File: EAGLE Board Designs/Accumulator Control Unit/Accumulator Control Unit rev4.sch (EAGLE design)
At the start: 244 parts, among them J1 CONNECTOR-2_MF_T_V_, J100 CONNECTOR-8_NF_T_V_NATURAL, J2 CONNECTOR-8_MF_T_V_, J3 CONNECTOR-14_MF_T_V_, J4 JUMPER__1X02, J5 CONNECTOR-12_MF_T_V_, J6 CONNECTOR-CAN_μF_S_RA_, J7 CONNECTOR-2_MOLEX_NANOFIT_PTH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, J8 JUMPER__1X02, K1 RELAY_SOLIDSTATE_NO_CPC1020NTR, Q1 TRANSISTOR_N_MOS__PMV15ENEA, Q100 TRANSISTOR_N_MOS__PMV15ENEA, Q101 TRANSISTOR_N_MOS__PMV15ENEA, Q2 TRANSISTOR_N_MOS__PMV15ENEA, T1 TRANSFORMER_HM2112ZNLT_AIRGAP, U1 RELAY_SOLIDSTATE_NO_DIP-4, U10 MAX7404, U100 ADG1423, U101 LM555, U11 OPAMP_1_CHANNEL_OPA991, U12 LOGICGATE_AND_DCK3, U13 OPAMP_1_CHANNEL_OPA991, U14 LOGICGATE_AND_DCK3, U15 OPAMP_1_CHANNEL_OPA991, U16 LOGICGATE_AND_DCK3, U17 OPAMP_1_CHANNEL_OPA991, U18 OPAMP_1_CHANNEL_OPA991, U19 MAX7404, U2 RELAY_SOLIDSTATE_NO_DIP-4, U20 OPAMP_1_CHANNEL_OPA991, U21 OPAMP_1_CHANNEL_OPA991, U22 OPAMP_1_CHANNEL_OPA991, U23 OPAMP_1_CHANNEL_OPA991, U24 OPAMP_1_CHANNEL_OPA991, U25 MAX7404, U26 VOLTAGE_REGULATOR_SOT-223_3.3V, U27 TCAN1051HQV-Q1, U28 OPAMP_1_CHANNEL_OPA991, U29 TCAN1051HQV-Q1, U3 OPAMP_1_CHANNEL_OPA991, U4 MAX7404, U5 LTC6820, U6 LOGICGATE_BUFFER, U7 ADM8316WBX30, U8 RELAY_SOLIDSTATE_NO_DIP-4, U9 OPAMP_1_CHANNEL_OPA991

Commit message: changes in progress
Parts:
- removed J7: CONNECTOR-2_MOLEX_NANOFIT_PTH_VERTICAL_02_BLACK, HyTechDevices:CONNECTOR-2_MOLEX_NANOFIT_PTH_VERTICAL_02_BLACK
- J5: value CONNECTOR-12_MF_T_V_ -> CONNECTOR-14_MF_T_V_; device HyTechDevices - Copy:CONNECTOR-12_MF_T_V_ -> HyTechDevices:CONNECTOR-14_MF_T_V_
- J6: value CONNECTOR-CAN_μF_S_RA_ -> CONNECTOR-4_μF_T_V_BLACK; device HyTechDevices:CONNECTOR-CAN_μF_S_RA_ -> HyTechDevices:CONNECTOR-4_μF_T_V_BLACK
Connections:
- net +24V: now also J6.1; no longer J5.1, J6.+24V
- net 24VIN: now also J5.1; no longer J7.1
- net CHASSIS_GND: now also J5.13; no longer J7.2
- net EM_CANH: now also J6.2; no longer J6.CANH
- net EM_CANL: now also J6.3; no longer J6.CANL
- net GND: now also J6.4; no longer J6.GND
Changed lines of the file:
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@@
 <part name="D4" library="HyTechDevices - Copy" deviceset="TVS_*" device="" technology="8V"/>
 <part name="P5" library="HyTechSupplies" deviceset="GND" device=""/>
-<part name="J6" library="HyTechDevices" deviceset="CONNECTOR-CAN_?_*" device="μF_S_RA"/>
-<part name="J5" library="HyTechDevices - Copy" deviceset="CONNECTOR-12_?_*" device="MF_T_V"/>
+<part name="J5" library="HyTechDevices" deviceset="CONNECTOR-14_?_*" device="MF_T_V"/>
 <part name="R12" library="HyTechDevices" deviceset="RESISTOR_?_*" device="0603" technology="20K" value="RESISTOR_0603_20K"/>
 <part name="GND5" library="supply1" library_urn="urn:adsk.eagle:library:371" deviceset="GND" device=""/>
@@
 <part name="R75" library="HyTechDevices" deviceset="RESISTOR_?_*" device="0603" technology="10.5K"/>
 <part name="R76" library="HyTechDevices" deviceset="RESISTOR_?_*" device="0603" technology="10.5K"/>
-<part name="U$29" library="HyTechSupplies" deviceset="+24V" device=""/>
-<part name="J7" library="HyTechDevices" deviceset="CONNECTOR-2_?_*" device="MOLEX_NANOFIT_PTH_VERTICAL_02" technology="BLACK"/>
 <part name="P115" library="HyTechSupplies" deviceset="GND" device=""/>
 <part name="U29" library="HyTechDevices" deviceset="TCAN1051*V-Q1" device="" technology="HQ"/>
@@
 <part name="P11" library="HyTechSupplies" deviceset="GND" device=""/>
 <part name="R92" library="HyTechDevices" deviceset="RESISTOR_?_*" device="0603" technology="10K"/>
+<part name="J6" library="HyTechDevices" deviceset="CONNECTOR-4_?_*" device="μF_T_V" technology="BLACK"/>
 </parts>
 <sheets>
@@
 <attribute name="VALUE" x="27.94" y="143.51" size="1.27" layer="96" align="top-center"/>
 </instance>
-<instance part="J6" gate="G$1" x="10.16" y="195.58" smashed="yes">
-<attribute name="NAME" x="10.16" y="196.215" size="1.27" layer="95"/>
-<attribute name="MPN" x="10.16" y="182.245" size="1.27" layer="96" align="top-left"/>
-</instance>
 <instance part="J5" gate="G$1" x="58.42" y="187.96" smashed="yes">
 <attribute name="NAME" x="58.42" y="188.722" size="1.778" layer="95"/>
-<attribute name="MPN" x="58.42" y="154.305" size="1.27" layer="96" align="top-left"/>
+<attribute name="MPN" x="58.42" y="149.225" size="1.27" layer="96" align="top-left"/>
 </instance>
 <instance part="P8" gate="G$1" x="27.94" y="68.58" smashed="yes">
@@
 <attribute name="VALUE" x="43.18" y="124.46" size="1.27" layer="96" align="bottom-center"/>
 </instance>
-<instance part="U$29" gate="G$1" x="83.82" y="187.96" smashed="yes">
-<attribute name="VALUE" x="83.82" y="193.04" size="1.778" layer="96" align="bottom-center"/>
-</instance>
-<instance part="J7" gate="G$1" x="58.42" y="142.24" smashed="yes">
-<attribute name="MPN" x="58.42" y="133.985" size="1.27" layer="96" align="top-left"/>
-<attribute name="NAME" x="58.42" y="143.002" size="1.27" layer="95"/>
-</instance>
-<instance part="P115" gate="1" x="76.2" y="152.4" smashed="yes">
-<attribute name="VALUE" x="76.2" y="151.13" size="1.27" layer="96" align="top-center"/>
+<instance part="P115" gate="1" x="93.98" y="154.94" smashed="yes">
+<attribute name="VALUE" x="93.98" y="153.67" size="1.27" layer="96" align="top-center"/>
 </instance>
 <instance part="K1" gate="G$1" x="83.82" y="58.42" smashed="yes">
@@
 <attribute name="NAME" x="74.93" y="57.15" size="1.27" layer="95" align="bottom-center"/>
 <attribute name="RESISTANCE" x="74.93" y="54.61" size="1.27" layer="96" align="top-center"/>
+</instance>
+<instance part="J6" gate="G$1" x="12.7" y="195.58" smashed="yes">
+<attribute name="MPN" x="12.7" y="182.245" size="1.27" layer="96" align="top-left"/>
+<attribute name="NAME" x="12.7" y="196.342" size="1.27" layer="95"/>
 </instance>
 </instances>
@@
 <wire x1="22.86" y1="185.42" x2="27.94" y2="185.42" width="0.1524" layer="91"/>
 <wire x1="27.94" y1="185.42" x2="27.94" y2="182.88" width="0.1524" layer="91"/>
-<pinref part="J6" gate="G$1" pin="GND"/>
+<pinref part="J6" gate="G$1" pin="4"/>
 </segment>
 <segment>
@@
 <pinref part="J5" gate="G$1" pin="12"/>
 <pinref part="P115" gate="1" pin="GND"/>
-<wire x1="68.58" y1="157.48" x2="76.2" y2="157.48" width="0.1524" layer="91"/>
-<wire x1="76.2" y1="157.48" x2="76.2" y2="154.94" width="0.1524" layer="91"/>
+<wire x1="68.58" y1="157.48" x2="93.98" y2="157.48" width="0.1524" layer="91"/>
 </segment>
 <segment>
@@
 </segment>
 <segment>
-<pinref part="J7" gate="G$1" pin="1"/>
-<wire x1="68.58" y1="139.7" x2="71.12" y2="139.7" width="0.1524" layer="91"/>
-<label x="71.12" y="139.7" size="1.27" layer="95" xref="yes"/>
+<pinref part="J5" gate="G$1" pin="1"/>
+<wire x1="68.58" y1="185.42" x2="83.82" y2="185.42" width="0.1524" layer="91"/>
+<label x="83.82" y="185.42" size="1.27" layer="95" xref="yes"/>
 </segment>
 </net>
@@
 </segment>
 <segment>
-<pinref part="J7" gate="G$1" pin="2"/>
-<wire x1="68.58" y1="137.16" x2="71.12" y2="137.16" width="0.1524" layer="91"/>
-<label x="71.12" y="137.16" size="1.27" layer="95" xref="yes"/>
+<pinref part="J5" gate="G$1" pin="13"/>
+<wire x1="68.58" y1="154.94" x2="76.2" y2="154.94" width="0.1524" layer="91"/>
+<label x="76.2" y="154.94" size="1.27" layer="95" xref="yes"/>
 </segment>
 </net>
@@
 <segment>
 <pinref part="P1" gate="G$1" pin="+24V"/>
-<pinref part="J6" gate="G$1" pin="+24V"/>
 <wire x1="27.94" y1="195.58" x2="27.94" y2="193.04" width="0.1524" layer="91"/>
 <wire x1="27.94" y1="193.04" x2="22.86" y2="193.04" width="0.1524" layer="91"/>
+<pinref part="J6" gate="G$1" pin="1"/>
 </segment>
 <segment>
@@
 </segment>
 <segment>
-<pinref part="J5" gate="G$1" pin="1"/>
-<pinref part="U$29" gate="G$1" pin="+24V"/>
-<wire x1="68.58" y1="185.42" x2="83.82" y2="185.42" width="0.1524" layer="91"/>
-</segment>
-<segment>
 <pinref part="U$30" gate="G$1" pin="+24V"/>
 <pinref part="K1" gate="G$1" pin="CONTACT2"/>
@@
 <wire x1="22.86" y1="190.5" x2="25.4" y2="190.5" width="0.1524" layer="91"/>
 <label x="25.4" y="190.5" size="1.27" layer="95" xref="yes"/>
-<pinref part="J6" gate="G$1" pin="CANH"/>
+<pinref part="J6" gate="G$1" pin="2"/>
 </segment>
 </net>
@@
 <wire x1="22.86" y1="187.96" x2="25.4" y2="187.96" width="0.1524" layer="91"/>
 <label x="25.4" y="187.96" size="1.27" layer="95" xref="yes"/>
-<pinref part="J6" gate="G$1" pin="CANL"/>
-</segment>
-</net>
+<pinref part="J6" gate="G$1" pin="3"/>
+</segment>
+</net>

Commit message: wip
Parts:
- J3: value CONNECTOR-14_MF_T_V_ -> CONNECTOR-12_MF_T_V_; device HyTechDevices:CONNECTOR-14_MF_T_V_ -> HyTechDevices:CONNECTOR-12_MF_T_V_
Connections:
- new net N$40: J3.10
- net +24V: now also J3.5; no longer J3.7
- net +5V: now also J3.3; no longer J3.5
- net ACCUMULATOR_GND: now also J3.12; no longer J3.14
- net AIR2-: now also J3.11; no longer J3.13
- net CURRENT: now also J3.6; no longer J3.8
- net CURRENT_REF: now also J3.7; no longer J3.9
- net GND: now also J3.2, J3.9; no longer J3.11, J3.6
- net SHDN: now also J3.8; no longer J3.10, J3.12
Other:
- note added: "Current Sensor Accumulator GND, both AIR+ and -"
- note removed: "Energy Meter, Current Sensor Accumulator GND, both AIR+ and -"
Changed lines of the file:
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@@
 <layer number="56" name="wert" color="7" fill="1" visible="no" active="no"/>
 <layer number="57" name="tCAD" color="7" fill="1" visible="no" active="no"/>
+<layer number="58" name="bCAD" color="7" fill="1" visible="no" active="no"/>
 <layer number="59" name="tCarbon" color="7" fill="1" visible="no" active="no"/>
 <layer number="60" name="bCarbon" color="7" fill="1" visible="no" active="no"/>
@@
 <layer number="156" name="HVSpacing" color="12" fill="1" visible="no" active="yes"/>
 <layer number="157" name="HIGH_VOLTAGE_WIRES" color="2" fill="1" visible="yes" active="yes"/>
+<layer number="166" name="AntennaArea" color="7" fill="1" visible="no" active="no"/>
+<layer number="168" name="4mmHeightArea" color="7" fill="1" visible="no" active="no"/>
 <layer number="191" name="mNets" color="7" fill="1" visible="no" active="yes"/>
 <layer number="192" name="mBusses" color="7" fill="1" visible="no" active="yes"/>
@@
 <part name="P109" library="HyTechSupplies" deviceset="+24V" device=""/>
 <part name="TP1_24V" library="HyTechDevices" deviceset="TEST_POINT" device=""/>
-<part name="J3" library="HyTechDevices" deviceset="CONNECTOR-14_?_*" device="MF_T_V"/>
 <part name="U$21" library="HyTechSupplies" deviceset="+24V" device=""/>
 <part name="P110" library="HyTechSupplies" deviceset="GND" device=""/>
@@
 <part name="R92" library="HyTechDevices" deviceset="RESISTOR_?_*" device="0603" technology="10K"/>
 <part name="J6" library="HyTechDevices" deviceset="CONNECTOR-4_?_*" device="μF_T_V" technology="BLACK"/>
+<part name="J3" library="HyTechDevices" deviceset="CONNECTOR-12_?_*" device="MF_T_V"/>
 </parts>
 <sheets>
@@
 <text x="30.988" y="105.156" size="0.8128" layer="97">SHDN connnects directly
 to AIR+</text>
-<text x="7.62" y="134.62" size="1.778" layer="97">Energy Meter, Current Sensor
+<text x="7.62" y="134.62" size="1.778" layer="97">Current Sensor
 Accumulator GND, both AIR+ and -</text>
 <text x="7.62" y="71.12" size="1.778" layer="97">IMD</text>
@@
 <attribute name="MPN" x="193.04" y="196.342" size="1.27" layer="95" align="top-left"/>
 </instance>
-<instance part="J3" gate="G$1" x="10.16" y="132.08" smashed="yes">
-<attribute name="NAME" x="10.16" y="132.842" size="1.27" layer="95"/>
-<attribute name="MPN" x="10.16" y="93.345" size="1.27" layer="96" align="top-left"/>
-</instance>
 <instance part="U$21" gate="G$1" x="101.6" y="160.02" smashed="yes">
 <attribute name="VALUE" x="101.6" y="165.1" size="1.778" layer="96" align="bottom-center"/>
@@
 <attribute name="VOLTAGE" x="121.285" y="184.15" size="1.27" layer="96" rot="R90" align="top-center"/>
 </instance>
-<instance part="P7" gate="1" x="43.18" y="121.92" smashed="yes">
-<attribute name="VALUE" x="43.18" y="124.46" size="1.27" layer="96" align="bottom-center"/>
+<instance part="P7" gate="1" x="40.64" y="121.92" smashed="yes">
+<attribute name="VALUE" x="43.18" y="121.92" size="1.27" layer="96" align="bottom-center"/>
 </instance>
 <instance part="P115" gate="1" x="93.98" y="154.94" smashed="yes">
@@
 <attribute name="MPN" x="12.7" y="182.245" size="1.27" layer="96" align="top-left"/>
 <attribute name="NAME" x="12.7" y="196.342" size="1.27" layer="95"/>
+</instance>
+<instance part="J3" gate="G$1" x="10.16" y="127" smashed="yes">
+<attribute name="NAME" x="10.16" y="127.762" size="1.778" layer="95"/>
+<attribute name="MPN" x="10.16" y="93.345" size="1.27" layer="96" align="top-left"/>
 </instance>
 </instances>
@@
 <wire x1="20.32" y1="106.68" x2="22.86" y2="106.68" width="0.1524" layer="91"/>
 <label x="22.86" y="106.68" size="1.27" layer="95" xref="yes"/>
-<pinref part="J3" gate="G$1" pin="10"/>
-</segment>
-<segment>
-<wire x1="20.32" y1="101.6" x2="22.86" y2="101.6" width="0.1524" layer="91"/>
-<label x="22.86" y="101.6" size="1.27" layer="95" xref="yes"/>
-<pinref part="J3" gate="G$1" pin="12"/>
+<pinref part="J3" gate="G$1" pin="8"/>
 </segment>
 </net>
@@
 </segment>
 <segment>
-<wire x1="20.32" y1="119.38" x2="43.18" y2="119.38" width="0.1524" layer="91"/>
-<pinref part="J3" gate="G$1" pin="5"/>
+<wire x1="20.32" y1="119.38" x2="40.64" y2="119.38" width="0.1524" layer="91"/>
 <pinref part="P7" gate="1" pin="+5V"/>
+<pinref part="J3" gate="G$1" pin="3"/>
 </segment>
 </net>
@@
 <wire x1="20.32" y1="121.92" x2="33.02" y2="121.92" width="0.1524" layer="91"/>
 <pinref part="P4" gate="1" pin="GND"/>
-<pinref part="J3" gate="G$1" pin="4"/>
+<pinref part="J3" gate="G$1" pin="2"/>
 </segment>
 <segment>
 <pinref part="P25" gate="1" pin="GND"/>
 <wire x1="20.32" y1="104.14" x2="38.1" y2="104.14" width="0.1524" layer="91"/>
-<pinref part="J3" gate="G$1" pin="11"/>
+<pinref part="J3" gate="G$1" pin="9"/>
 </segment>
 <segment>
@@
 <wire x1="20.32" y1="116.84" x2="45.974" y2="116.84" width="0.1524" layer="91"/>
 <pinref part="P9" gate="1" pin="GND"/>
-<pinref part="J3" gate="G$1" pin="6"/>
+<pinref part="J3" gate="G$1" pin="4"/>
 </segment>
 <segment>
@@
 <wire x1="20.32" y1="96.52" x2="22.86" y2="96.52" width="0.1524" layer="91"/>
 <label x="22.86" y="96.52" size="1.27" layer="95" xref="yes"/>
-<pinref part="J3" gate="G$1" pin="14"/>
+<pinref part="J3" gate="G$1" pin="12"/>
 </segment>
 </net>
@@
 <wire x1="20.32" y1="99.06" x2="22.86" y2="99.06" width="0.1524" layer="91"/>
 <label x="22.86" y="99.06" size="1.27" layer="95" xref="yes"/>
-<pinref part="J3" gate="G$1" pin="13"/>
+<pinref part="J3" gate="G$1" pin="11"/>
 </segment>
 </net>
@@
 <wire x1="20.32" y1="109.22" x2="22.86" y2="109.22" width="0.1524" layer="91"/>
 <label x="22.86" y="109.22" size="1.27" layer="95" xref="yes"/>
-<pinref part="J3" gate="G$1" pin="9"/>
+<pinref part="J3" gate="G$1" pin="7"/>
 </segment>
 <segment>
@@
 <wire x1="20.32" y1="111.76" x2="22.86" y2="111.76" width="0.1524" layer="91"/>
 <label x="22.86" y="111.76" size="1.27" layer="95" xref="yes"/>
-<pinref part="J3" gate="G$1" pin="8"/>
+<pinref part="J3" gate="G$1" pin="6"/>
 </segment>
 <segment>
@@
 <pinref part="P3" gate="G$1" pin="+24V"/>
 <wire x1="20.32" y1="114.3" x2="53.34" y2="114.3" width="0.1524" layer="91"/>
-<pinref part="J3" gate="G$1" pin="7"/>
+<pinref part="J3" gate="G$1" pin="5"/>
 </segment>
 <segment>
@@
 <net name="INVERTER_24V" class="0">
 <segment>
-<pinref part="J3" gate="G$1" pin="1"/>
-<wire x1="20.32" y1="129.54" x2="33.02" y2="129.54" width="0.1524" layer="91"/>
-<label x="33.02" y="129.54" size="1.27" layer="95" xref="yes"/>
-</segment>
-<segment>
 <pinref part="K1" gate="G$1" pin="CONTACT1"/>
 <wire x1="104.14" y1="48.26" x2="109.22" y2="48.26" width="0.1524" layer="91"/>
 <label x="109.22" y="48.26" size="1.27" layer="95" xref="yes"/>
 </segment>
+<segment>
+<pinref part="J3" gate="G$1" pin="1"/>
+<wire x1="20.32" y1="124.46" x2="45.72" y2="124.46" width="0.1524" layer="91"/>
+<label x="45.72" y="124.46" size="1.27" layer="95" xref="yes"/>
+</segment>
 </net>
 <net name="N$38" class="0">
@@
 </segment>
 </net>
+<net name="N$40" class="0">
+<segment>
+<wire x1="20.32" y1="101.6" x2="22.86" y2="101.6" width="0.1524" layer="91"/>
+<label x="22.86" y="101.6" size="1.27" layer="95" xref="yes"/>
+<pinref part="J3" gate="G$1" pin="10"/>
+</segment>
+</net>

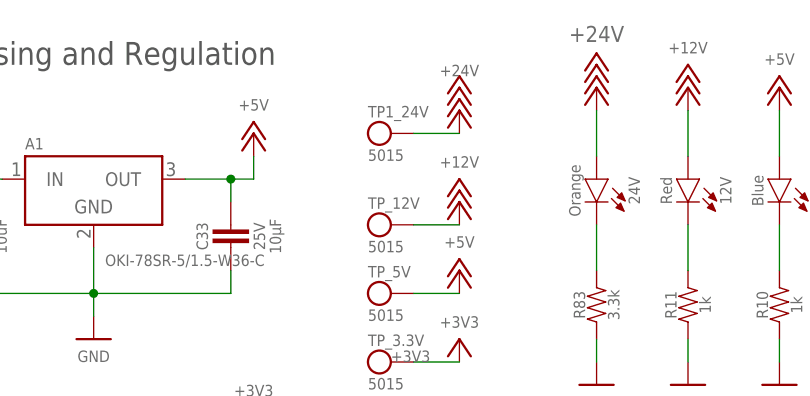
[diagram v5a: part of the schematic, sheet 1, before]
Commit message: parts placement done, routing in progress
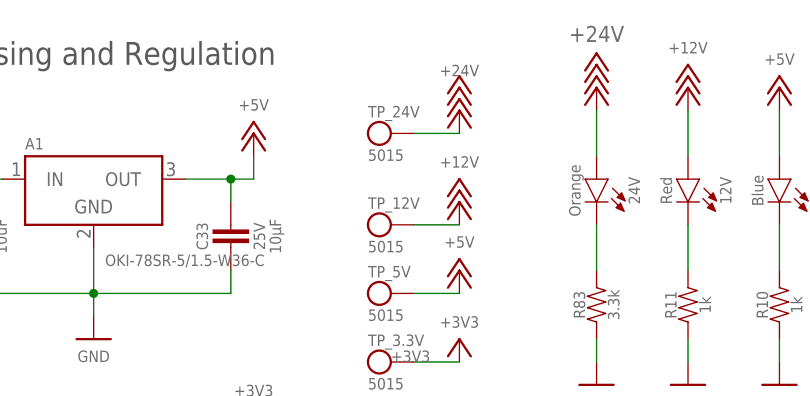
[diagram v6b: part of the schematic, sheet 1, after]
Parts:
- renumbered TP1_24V to TP_24V
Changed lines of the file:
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@@
 <part name="A3" library="HyTechDevices" deviceset="VOLTAGE_REGULATOR_MODULE_?_*" device="OKI-78SR" technology="12V"/>
 <part name="P109" library="HyTechSupplies" deviceset="+24V" device=""/>
-<part name="TP1_24V" library="HyTechDevices" deviceset="TEST_POINT" device=""/>
+<part name="TP_24V" library="HyTechDevices" deviceset="TEST_POINT" device=""/>
 <part name="U$21" library="HyTechSupplies" deviceset="+24V" device=""/>
 <part name="P110" library="HyTechSupplies" deviceset="GND" device=""/>
@@
 <attribute name="VALUE" x="203.2" y="204.47" size="1.27" layer="96" align="bottom-center"/>
 </instance>
-<instance part="TP1_24V" gate="G$1" x="195.58" y="198.12" smashed="yes">
+<instance part="TP_24V" gate="G$1" x="195.58" y="198.12" smashed="yes">
 <attribute name="NAME" x="193.04" y="199.898" size="1.27" layer="95"/>
 <attribute name="MPN" x="193.04" y="196.342" size="1.27" layer="95" align="top-left"/>
@@
 <segment>
 <pinref part="P109" gate="G$1" pin="+24V"/>
-<pinref part="TP1_24V" gate="G$1" pin="1"/>
+<pinref part="TP_24V" gate="G$1" pin="1"/>
 <wire x1="203.2" y1="198.12" x2="198.12" y2="198.12" width="0.1524" layer="91"/>
 </segment>

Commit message: work in progress
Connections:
- removed net N$40: J3.10
- net SHDN: now also J3.10
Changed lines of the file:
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@@
 <pinref part="J3" gate="G$1" pin="8"/>
+</segment>
+<segment>
+<wire x1="20.32" y1="101.6" x2="22.86" y2="101.6" width="0.1524" layer="91"/>
+<label x="22.86" y="101.6" size="1.27" layer="95" xref="yes"/>
+<pinref part="J3" gate="G$1" pin="10"/>
 </segment>
 </net>
@@
 </segment>
 </net>
-<net name="N$40" class="0">
-<segment>
-<wire x1="20.32" y1="101.6" x2="22.86" y2="101.6" width="0.1524" layer="91"/>
-<label x="22.86" y="101.6" size="1.27" layer="95" xref="yes"/>
-<pinref part="J3" gate="G$1" pin="10"/>
-</segment>
-</net>

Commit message: minor changes
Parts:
- TP_24V: SIGNAL (none) -> +24V
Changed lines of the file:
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@@
 <part name="A3" library="HyTechDevices" deviceset="VOLTAGE_REGULATOR_MODULE_?_*" device="OKI-78SR" technology="12V"/>
 <part name="P109" library="HyTechSupplies" deviceset="+24V" device=""/>
-<part name="TP_24V" library="HyTechDevices" deviceset="TEST_POINT" device=""/>
 <part name="U$21" library="HyTechSupplies" deviceset="+24V" device=""/>
 <part name="P110" library="HyTechSupplies" deviceset="GND" device=""/>
@@
 <part name="J6" library="HyTechDevices" deviceset="CONNECTOR-4_?_*" device="μF_T_V" technology="BLACK"/>
 <part name="J3" library="HyTechDevices" deviceset="CONNECTOR-12_?_*" device="MF_T_V"/>
+<part name="TP_24V" library="HyTechDevices" deviceset="TEST_POINT" device="">
+<attribute name="SIGNAL" value="+24V"/>
+</part>
 </parts>
 <sheets>
@@
 <attribute name="VALUE" x="203.2" y="204.47" size="1.27" layer="96" align="bottom-center"/>
 </instance>
-<instance part="TP_24V" gate="G$1" x="195.58" y="198.12" smashed="yes">
-<attribute name="NAME" x="193.04" y="199.898" size="1.27" layer="95"/>
-<attribute name="MPN" x="193.04" y="196.342" size="1.27" layer="95" align="top-left"/>
-</instance>
 <instance part="U$21" gate="G$1" x="101.6" y="160.02" smashed="yes">
 <attribute name="VALUE" x="101.6" y="165.1" size="1.778" layer="96" align="bottom-center"/>
@@
 <attribute name="NAME" x="10.16" y="127.762" size="1.778" layer="95"/>
 <attribute name="MPN" x="10.16" y="93.345" size="1.27" layer="96" align="top-left"/>
+</instance>
+<instance part="TP_24V" gate="G$1" x="195.58" y="198.12" smashed="yes">
+<attribute name="NAME" x="193.04" y="199.898" size="1.27" layer="95"/>
+<attribute name="MPN" x="193.04" y="196.342" size="1.27" layer="95" align="top-left"/>
+<attribute name="SIGNAL" x="195.58" y="198.12" size="1.27" layer="96" display="off"/>
 </instance>
 </instances>
@@
 <segment>
 <pinref part="P109" gate="G$1" pin="+24V"/>
+<wire x1="203.2" y1="198.12" x2="198.12" y2="198.12" width="0.1524" layer="91"/>
 <pinref part="TP_24V" gate="G$1" pin="1"/>
-<wire x1="203.2" y1="198.12" x2="198.12" y2="198.12" width="0.1524" layer="91"/>
-</segment>
-<segment>
+</segment>
+<segment>
